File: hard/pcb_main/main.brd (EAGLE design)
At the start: 230 x 150 mm, 866 parts

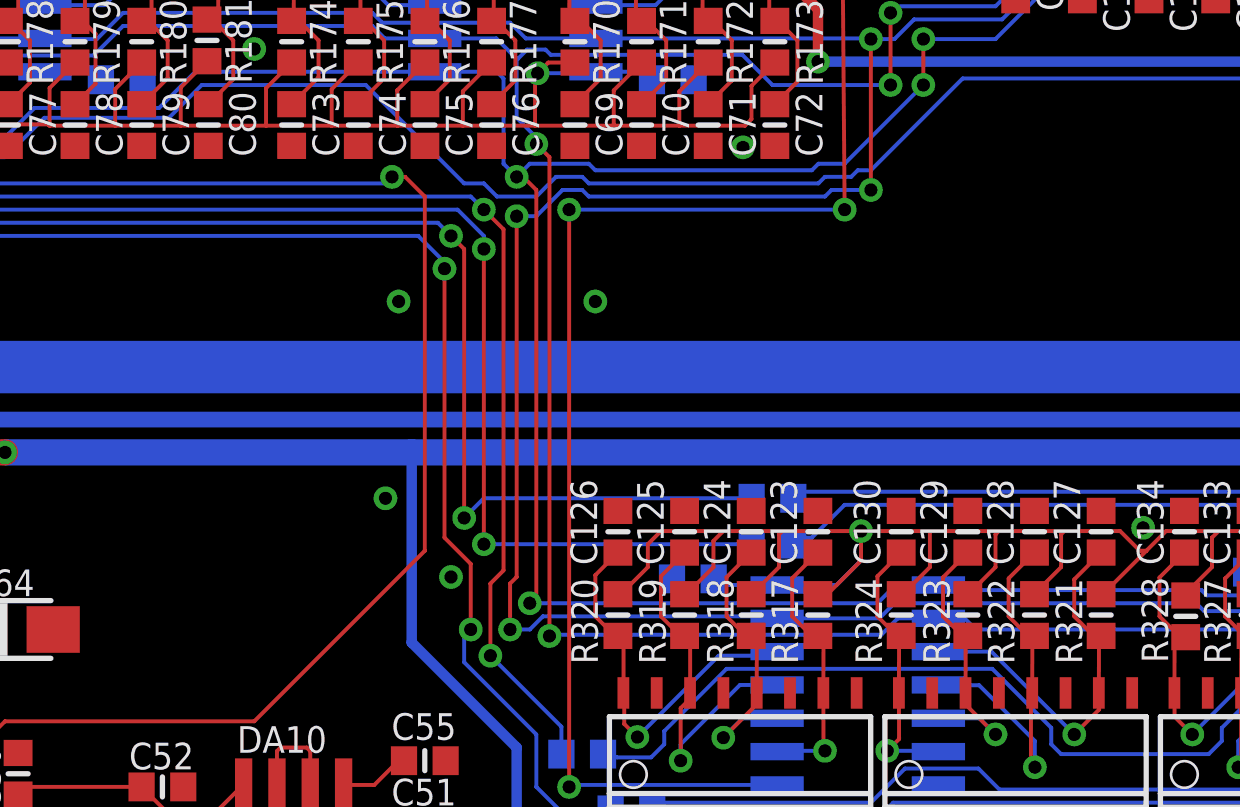
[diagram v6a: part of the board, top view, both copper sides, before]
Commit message: added 2 additional mount holes
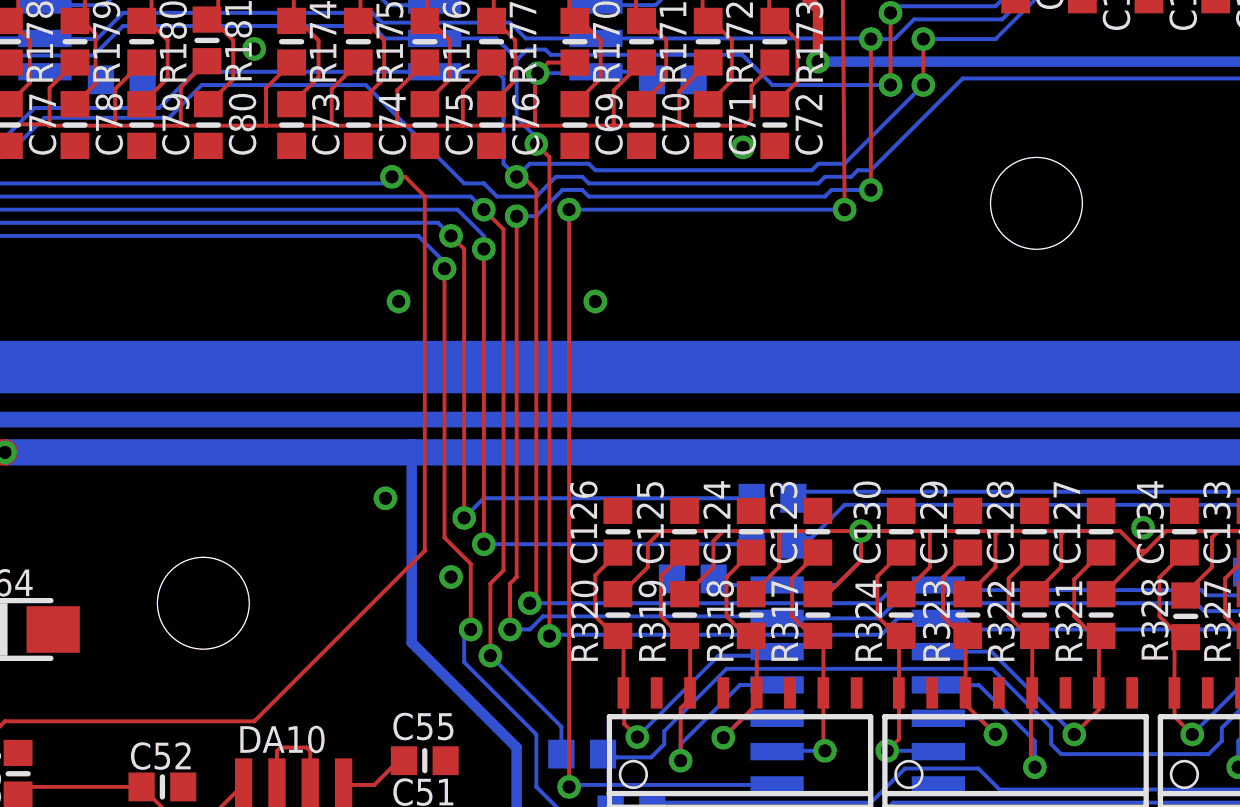
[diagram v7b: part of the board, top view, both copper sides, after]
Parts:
- added JP10, JP9: STAND-OFF-M4, mount:STAND-OFF
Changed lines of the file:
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@@
 <layer number="23" name="tOrigins" color="15" fill="1" visible="yes" active="yes"/>
 <layer number="24" name="bOrigins" color="15" fill="1" visible="yes" active="yes"/>
-<layer number="25" name="tNames" color="7" fill="1" visible="yes" active="yes"/>
+<layer number="25" name="tNames" color="7" fill="1" visible="no" active="yes"/>
 <layer number="26" name="bNames" color="15" fill="1" visible="no" active="yes"/>
 <layer number="27" name="tValues" color="7" fill="1" visible="no" active="yes"/>
 <layer number="28" name="bValues" color="7" fill="1" visible="no" active="yes"/>
-<layer number="29" name="tStop" color="7" fill="3" visible="yes" active="yes"/>
+<layer number="29" name="tStop" color="7" fill="3" visible="no" active="yes"/>
 <layer number="30" name="bStop" color="15" fill="6" visible="no" active="yes"/>
 <layer number="31" name="tCream" color="7" fill="4" visible="no" active="yes"/>
@@
 <layer number="46" name="Milling" color="3" fill="1" visible="no" active="yes"/>
 <layer number="47" name="Measures" color="7" fill="1" visible="no" active="yes"/>
-<layer number="48" name="Document" color="7" fill="1" visible="no" active="yes"/>
+<layer number="48" name="Document" color="7" fill="1" visible="yes" active="yes"/>
 <layer number="49" name="Reference" color="7" fill="1" visible="no" active="yes"/>
 <layer number="50" name="dxf" color="7" fill="1" visible="no" active="no"/>
@@
 <attribute name="VALUE" x="65.5675" y="68.3725" size="0.8128" layer="27"/>
 </element>
+<element name="JP9" library="mount" package="STAND-OFF" value="STAND-OFF-M4" x="130.81" y="78.74">
+<attribute name="DATABASE" value="./bom/volat3-PARTSDB.tsv" x="130.81" y="78.74" size="1.778" layer="27" display="off"/>
+</element>
+<element name="JP10" library="mount" package="STAND-OFF" value="STAND-OFF-M4" x="99.06" y="63.5">
+<attribute name="DATABASE" value="./bom/volat3-PARTSDB.tsv" x="99.06" y="63.5" size="1.778" layer="27" display="off"/>
+</element>
 </elements>

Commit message: nets renamed
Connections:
- net RAW_DISCRETE_1 renamed REL_RAW_1
- net RAW_DISCRETE_10 renamed REL_RAW_10
- net RAW_DISCRETE_11 renamed REL_RAW_11
- net RAW_DISCRETE_12 renamed REL_RAW_12
- net RAW_DISCRETE_13 renamed REL_RAW_13
- net RAW_DISCRETE_14 renamed REL_RAW_14
- net RAW_DISCRETE_15 renamed REL_RAW_15
- net RAW_DISCRETE_16 renamed REL_RAW_16
- net RAW_DISCRETE_17 renamed REL_RAW_17
- net RAW_DISCRETE_18 renamed REL_RAW_18
- net RAW_DISCRETE_19 renamed REL_RAW_19
- net RAW_DISCRETE_2 renamed REL_RAW_2
- net RAW_DISCRETE_20 renamed REL_RAW_20
- net RAW_DISCRETE_21 renamed REL_RAW_21
- net RAW_DISCRETE_22 renamed REL_RAW_22
- net RAW_DISCRETE_23 renamed REL_RAW_23
- net RAW_DISCRETE_24 renamed REL_RAW_24
- net RAW_DISCRETE_25 renamed REL_RAW_25
- net RAW_DISCRETE_26 renamed REL_RAW_26
- net RAW_DISCRETE_27 renamed REL_RAW_27
- net RAW_DISCRETE_28 renamed REL_RAW_28
- net RAW_DISCRETE_29 renamed REL_RAW_29
- net RAW_DISCRETE_3 renamed REL_RAW_3
- net RAW_DISCRETE_30 renamed REL_RAW_30
- net RAW_DISCRETE_31 renamed REL_RAW_31
- net RAW_DISCRETE_32 renamed REL_RAW_32
- net RAW_DISCRETE_33 renamed REL_RAW_33
- net RAW_DISCRETE_34 renamed REL_RAW_34
- net RAW_DISCRETE_35 renamed REL_RAW_35
- net RAW_DISCRETE_36 renamed REL_RAW_36
- net RAW_DISCRETE_37 renamed REL_RAW_37
- net RAW_DISCRETE_38 renamed REL_RAW_38
- net RAW_DISCRETE_39 renamed REL_RAW_39
- net RAW_DISCRETE_4 renamed REL_RAW_4
- net RAW_DISCRETE_40 renamed REL_RAW_40
- net RAW_DISCRETE_41 renamed REL_RAW_41
- net RAW_DISCRETE_42 renamed REL_RAW_42
- net RAW_DISCRETE_43 renamed REL_RAW_43
- net RAW_DISCRETE_44 renamed REL_RAW_44
- net RAW_DISCRETE_45 renamed REL_RAW_45
- net RAW_DISCRETE_46 renamed REL_RAW_46
- net RAW_DISCRETE_47 renamed REL_RAW_47
- net RAW_DISCRETE_48 renamed REL_RAW_48
- net RAW_DISCRETE_49 renamed REL_RAW_49
- net RAW_DISCRETE_5 renamed REL_RAW_5
- net RAW_DISCRETE_50 renamed REL_RAW_50
- net RAW_DISCRETE_51 renamed REL_RAW_51
- net RAW_DISCRETE_52 renamed REL_RAW_52
- net RAW_DISCRETE_53 renamed REL_RAW_53
- net RAW_DISCRETE_54 renamed REL_RAW_54
- net RAW_DISCRETE_55 renamed REL_RAW_55
- net RAW_DISCRETE_56 renamed REL_RAW_56
- net RAW_DISCRETE_57 renamed REL_RAW_57
- net RAW_DISCRETE_58 renamed REL_RAW_58
- net RAW_DISCRETE_59 renamed REL_RAW_59
- net RAW_DISCRETE_6 renamed REL_RAW_6
- net RAW_DISCRETE_60 renamed REL_RAW_60
- net RAW_DISCRETE_61 renamed REL_RAW_61
- net RAW_DISCRETE_62 renamed REL_RAW_62
- net RAW_DISCRETE_63 renamed REL_RAW_63
- net RAW_DISCRETE_64 renamed REL_RAW_64
- net RAW_DISCRETE_7 renamed REL_RAW_7
- net RAW_DISCRETE_8 renamed REL_RAW_8
- net RAW_DISCRETE_9 renamed REL_RAW_9
- removed net AN_RAW_0: R26.2, VD12.A, VD4.A1, XP4.10
- new net AN_RAW_2_SUPPLY: R28.2, VD14.A, VD6.A1
- net AN_FILTERED_0: now also DD1.23, Z24.3; no longer DD1.15, Z22.3
- net AN_FILTERED_1: now also DD1.24, Z27.3; no longer DD1.16, Z23.3
- net AN_FILTERED_10: now also DD1.15, Z22.3; no longer DD1.33, Z32.3
- net AN_FILTERED_11: now also DD1.16, Z23.3; no longer DD1.31, Z33.3
- net AN_FILTERED_12: now also DD1.17, Z25.3; no longer DD1.32, Z34.3
- net AN_FILTERED_13: now also DD1.18, Z26.3; no longer DD1.34, Z35.3
- net AN_FILTERED_14: now also DD1.33, Z32.3; no longer DD1.36, Z36.3
- net AN_FILTERED_15: now also DD1.34, Z35.3; no longer DD1.35, Z37.3
- net AN_FILTERED_2: now also DD1.25, Z29.3; no longer DD1.23, Z24.3
- net AN_FILTERED_3: now also DD1.26, Z28.3; no longer DD1.17, Z25.3
- net AN_FILTERED_4: now also DD1.29, Z30.3; no longer DD1.18, Z26.3
- net AN_FILTERED_5: now also DD1.30, Z31.3; no longer DD1.24, Z27.3
- net AN_FILTERED_6: now also DD1.31, Z33.3; no longer DD1.26, Z28.3
- net AN_FILTERED_7: now also DD1.32, Z34.3; no longer DD1.25, Z29.3
- net AN_FILTERED_8: now also DD1.35, Z37.3; no longer DD1.29, Z30.3
- net AN_FILTERED_9: now also DD1.36, Z36.3; no longer DD1.30, Z31.3
- net AN_RAW_1: now also R31.2, VD17.A, VD9.A1, XP4.1; no longer R27.2, VD13.A, VD5.A1, XP4.11
- net AN_RAW_10: now also R26.2, VD12.A, VD4.A1, XP4.10; no longer R52.2, VD22.A1, VD30.A, XP4.14
- net AN_RAW_11: now also R27.2, VD13.A, VD5.A1, XP4.11; no longer R53.2, VD23.A1, VD31.A, XP4.6
- net AN_RAW_12: now also R29.2, VD15.A, VD7.A1, XP4.12; no longer R54.2, VD24.A1, VD32.A, XP4.7
- net AN_RAW_13: now also R30.2, VD16.A, VD8.A1, XP4.13; no longer R55.2, VD25.A1, VD33.A, XP4.15
- net AN_RAW_14: now also R52.2, VD22.A1, VD30.A, XP4.14; no longer R56.2, VD26.A1, VD34.A, XP4.9
- net AN_RAW_15: now also R55.2, VD25.A1, VD33.A, XP4.15; no longer R57.2, VD27.A1, VD35.A, XP4.8
- net AN_RAW_2: now also R33.2, VD11.A1, VD19.A, XP4.2; no longer R28.2, VD14.A, VD6.A1
- net AN_RAW_3: now also R32.2, VD10.A1, VD18.A, XP4.3; no longer R29.2, VD15.A, VD7.A1, XP4.12
- net AN_RAW_4: now also R50.2, VD20.A1, VD28.A, XP4.4; no longer R30.2, VD16.A, VD8.A1, XP4.13
- net AN_RAW_5: now also R51.2, VD21.A1, VD29.A, XP4.5; no longer R31.2, VD17.A, VD9.A1, XP4.1
- net AN_RAW_6: now also R53.2, VD23.A1, VD31.A, XP4.6; no longer R32.2, VD10.A1, VD18.A, XP4.3
- net AN_RAW_7: now also R54.2, VD24.A1, VD32.A, XP4.7; no longer R33.2, VD11.A1, VD19.A, XP4.2
- net AN_RAW_8: now also R57.2, VD27.A1, VD35.A, XP4.8; no longer R50.2, VD20.A1, VD28.A, XP4.4
- net AN_RAW_9: now also R56.2, VD26.A1, VD34.A, XP4.9; no longer R51.2, VD21.A1, VD29.A, XP4.5
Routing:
- net AN_RAW_0: track 47.2 -> 0.00 mm, vias 4 -> 0
- net AN_RAW_2_SUPPLY: track 0.00 -> 21.9 mm, vias 0 -> 2
- net AN_RAW_14: track 58.9 -> 38.3 mm
- net AN_RAW_7: track 30.9 -> 51.4 mm
- net AN_RAW_5: track 42.2 -> 57.7 mm
- net AN_FILTERED_8: track 11.6 -> 26.0 mm
- net AN_FILTERED_9: track 13.2 -> 26.4 mm
- net AN_FILTERED_3: track 21.5 -> 9.49 mm
- net AN_RAW_13: track 46.4 -> 58.4 mm
- net AN_FILTERED_1: track 24.9 -> 13.1 mm
- net AN_RAW_1: track 52.9 -> 42.2 mm, vias 3 -> 2
- net AN_FILTERED_11: track 14.9 -> 24.9 mm
- net AN_RAW_11: track 43.5 -> 52.9 mm, vias 2 -> 3
- net AN_FILTERED_0: track 26.2 -> 16.8 mm
- net AN_RAW_2: track 21.9 -> 30.9 mm
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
